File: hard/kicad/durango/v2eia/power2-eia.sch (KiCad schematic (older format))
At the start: 73 parts, among them J11 EXPANSION, J4 LED, J605 COMPONENT VIDEO, J7 POWER IN, J706 COMPOSITE, J8 DEBUG, J9 CARTRIDGE, Q608 BC548, Q609 BC548, Q610 BC548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

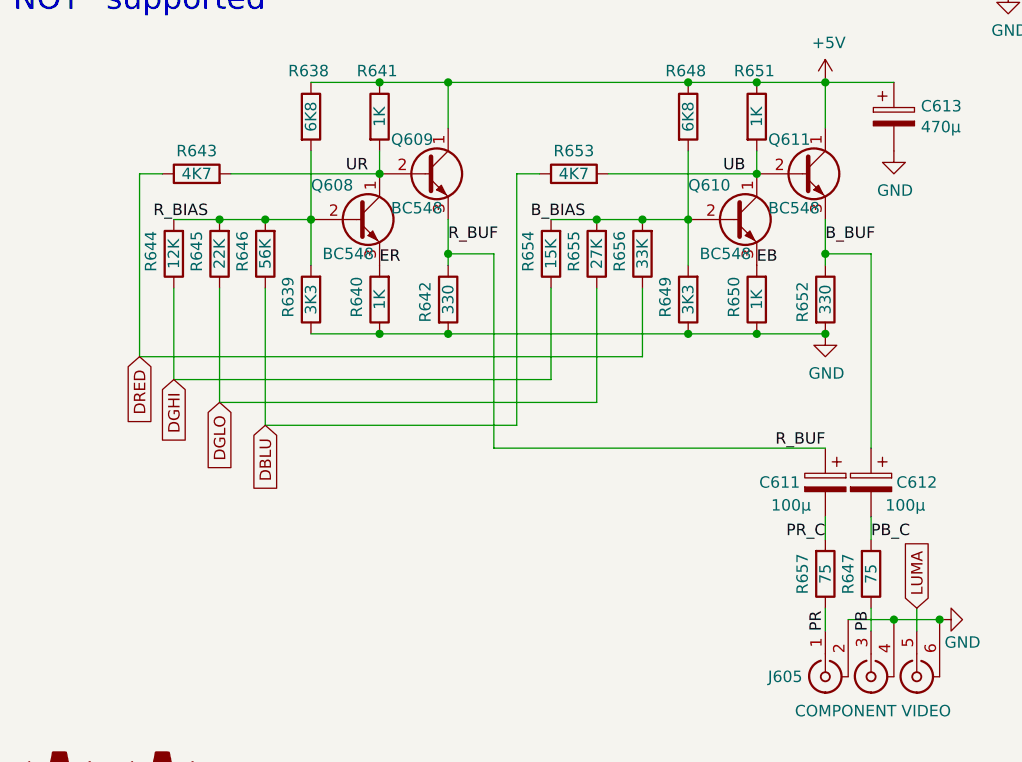
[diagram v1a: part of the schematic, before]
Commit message: fix YUV values for EIA
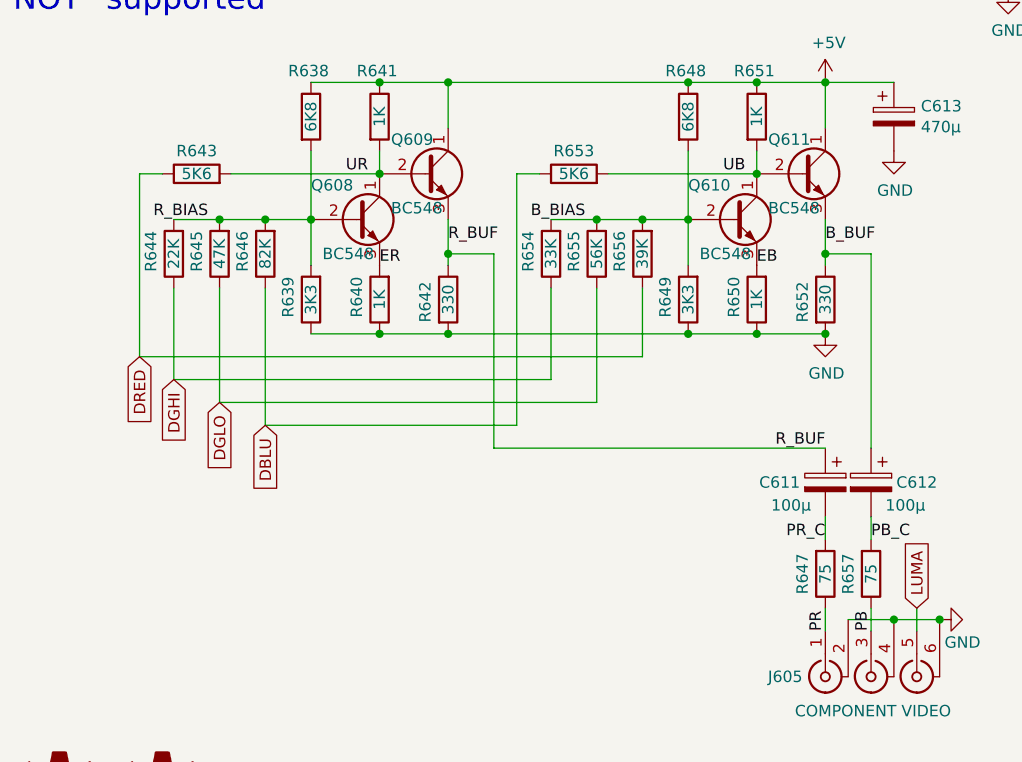
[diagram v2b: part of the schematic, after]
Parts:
- R643, R653: value 4K7 -> 5K6
- R644: value 12K -> 22K
- R645: value 22K -> 47K
- R646: value 56K -> 82K
- R654: value 15K -> 33K
- R655: value 27K -> 56K
- R656: value 33K -> 39K
- renumbered R657 to R647, R647 to R657
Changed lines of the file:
@@
 P 7050 4250
 F 0 "R646" V 7150 4150 50  0000 L CNN
-F 1 "56K" V 7050 4250 50  0000 C CNN
+F 1 "82K" V 7050 4250 50  0000 C CNN
 F 2 "Resistor_THT:R_Axial_DIN0207_L6.3mm_D2.5mm_P2.54mm_Vertical" V 6980 4250 50  0001 C CNN
 F 3 "~" H 7050 4250 50  0001 C CNN
@@
 P 6850 4250
 F 0 "R645" V 6950 4150 50  0000 L CNN
-F 1 "22K" V 6850 4250 50  0000 C CNN
+F 1 "47K" V 6850 4250 50  0000 C CNN
 F 2 "Resistor_THT:R_Axial_DIN0207_L6.3mm_D2.5mm_P2.54mm_Vertical" V 6780 4250 50  0001 C CNN
 F 3 "~" H 6850 4250 50  0001 C CNN
@@
 P 6650 4250
 F 0 "R644" V 6750 4150 50  0000 L CNN
-F 1 "12K" V 6650 4250 50  0000 C CNN
+F 1 "22K" V 6650 4250 50  0000 C CNN
 F 2 "Resistor_THT:R_Axial_DIN0207_L6.3mm_D2.5mm_P2.54mm_Vertical" V 6580 4250 50  0001 C CNN
 F 3 "~" H 6650 4250 50  0001 C CNN
@@
 P 6750 3900
 F 0 "R643" V 6850 3900 50  0000 C CNN
-F 1 "4K7" V 6750 3900 50  0000 C CNN
+F 1 "5K6" V 6750 3900 50  0000 C CNN
 F 2 "Resistor_THT:R_Axial_DIN0207_L6.3mm_D2.5mm_P2.54mm_Vertical" V 6680 3900 50  0001 C CNN
 F 3 "~" H 6750 3900 50  0001 C CNN
@@
 $EndComp
 $Comp
-L Device:R R657
+L Device:R R647
 U 1 1 65030F60
 P 9500 5650
-F 0 "R657" V 9400 5650 50  0000 C CNN
+F 0 "R647" V 9400 5650 50  0000 C CNN
 F 1 "75" V 9500 5650 50  0000 C CNN
 F 2 "Resistor_THT:R_Axial_DIN0207_L6.3mm_D2.5mm_P2.54mm_Vertical" V 9430 5650 50  0001 C CNN
@@
 $EndComp
 $Comp
-L Device:R R647
+L Device:R R657
 U 1 1 65031F66
 P 9700 5650
-F 0 "R647" V 9600 5650 50  0000 C CNN
+F 0 "R657" V 9600 5650 50  0000 C CNN
 F 1 "75" V 9700 5650 50  0000 C CNN
 F 2 "Resistor_THT:R_Axial_DIN0207_L6.3mm_D2.5mm_P2.54mm_Vertical" V 9630 5650 50  0001 C CNN
@@
 P 8700 4250
 F 0 "R656" V 8800 4150 50  0000 L CNN
-F 1 "33K" V 8700 4250 50  0000 C CNN
+F 1 "39K" V 8700 4250 50  0000 C CNN
 F 2 "Resistor_THT:R_Axial_DIN0207_L6.3mm_D2.5mm_P2.54mm_Vertical" V 8630 4250 50  0001 C CNN
 F 3 "~" H 8700 4250 50  0001 C CNN
@@
 P 8500 4250
 F 0 "R655" V 8600 4150 50  0000 L CNN
-F 1 "27K" V 8500 4250 50  0000 C CNN
+F 1 "56K" V 8500 4250 50  0000 C CNN
 F 2 "Resistor_THT:R_Axial_DIN0207_L6.3mm_D2.5mm_P2.54mm_Vertical" V 8430 4250 50  0001 C CNN
 F 3 "~" H 8500 4250 50  0001 C CNN
@@
 P 8300 4250
 F 0 "R654" V 8400 4150 50  0000 L CNN
-F 1 "15K" V 8300 4250 50  0000 C CNN
+F 1 "33K" V 8300 4250 50  0000 C CNN
 F 2 "Resistor_THT:R_Axial_DIN0207_L6.3mm_D2.5mm_P2.54mm_Vertical" V 8230 4250 50  0001 C CNN
 F 3 "~" H 8300 4250 50  0001 C CNN
@@
 P 8400 3900
 F 0 "R653" V 8500 3900 50  0000 C CNN
-F 1 "4K7" V 8400 3900 50  0000 C CNN
+F 1 "5K6" V 8400 3900 50  0000 C CNN
 F 2 "Resistor_THT:R_Axial_DIN0207_L6.3mm_D2.5mm_P2.54mm_Vertical" V 8330 3900 50  0001 C CNN
 F 3 "~" H 8400 3900 50  0001 C CNN
